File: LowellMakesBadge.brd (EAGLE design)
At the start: 51.9 x 52 mm, 2 parts

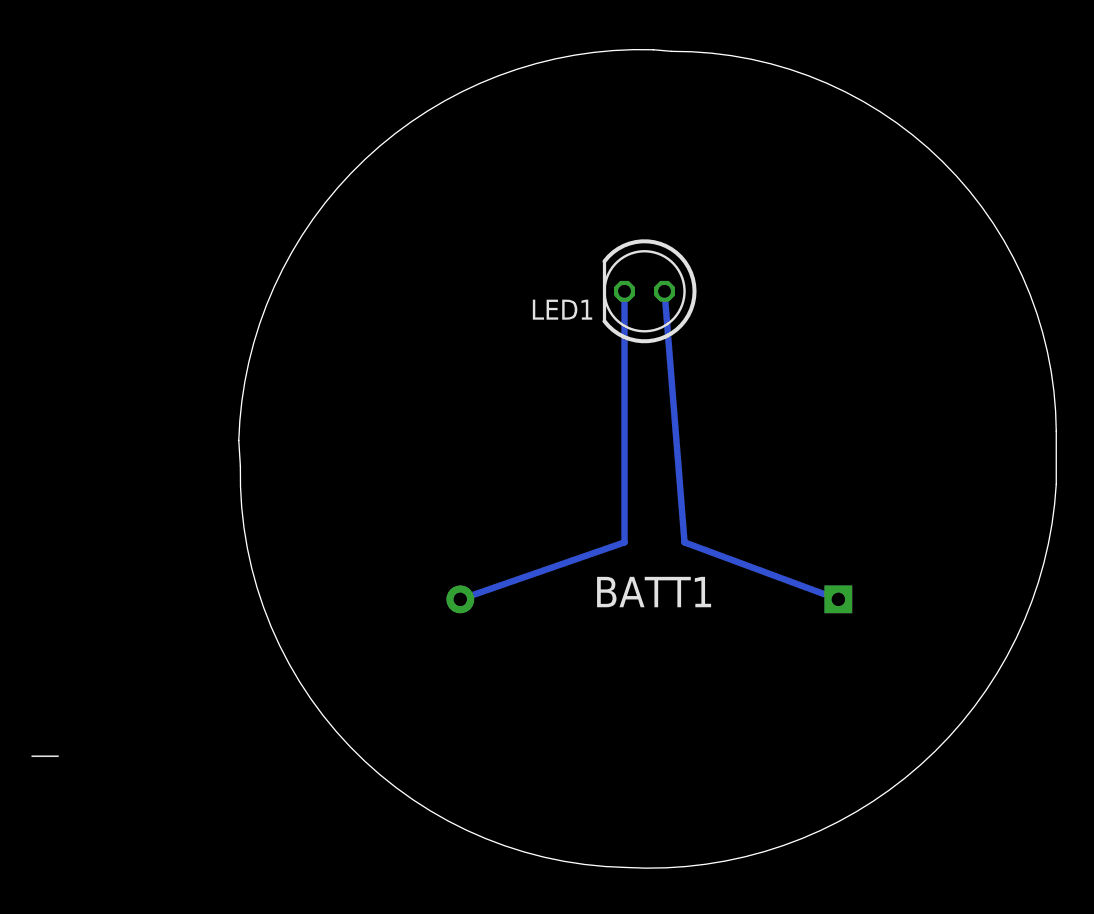
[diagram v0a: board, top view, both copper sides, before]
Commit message: Adding next version from @sajingeo including a 3d model
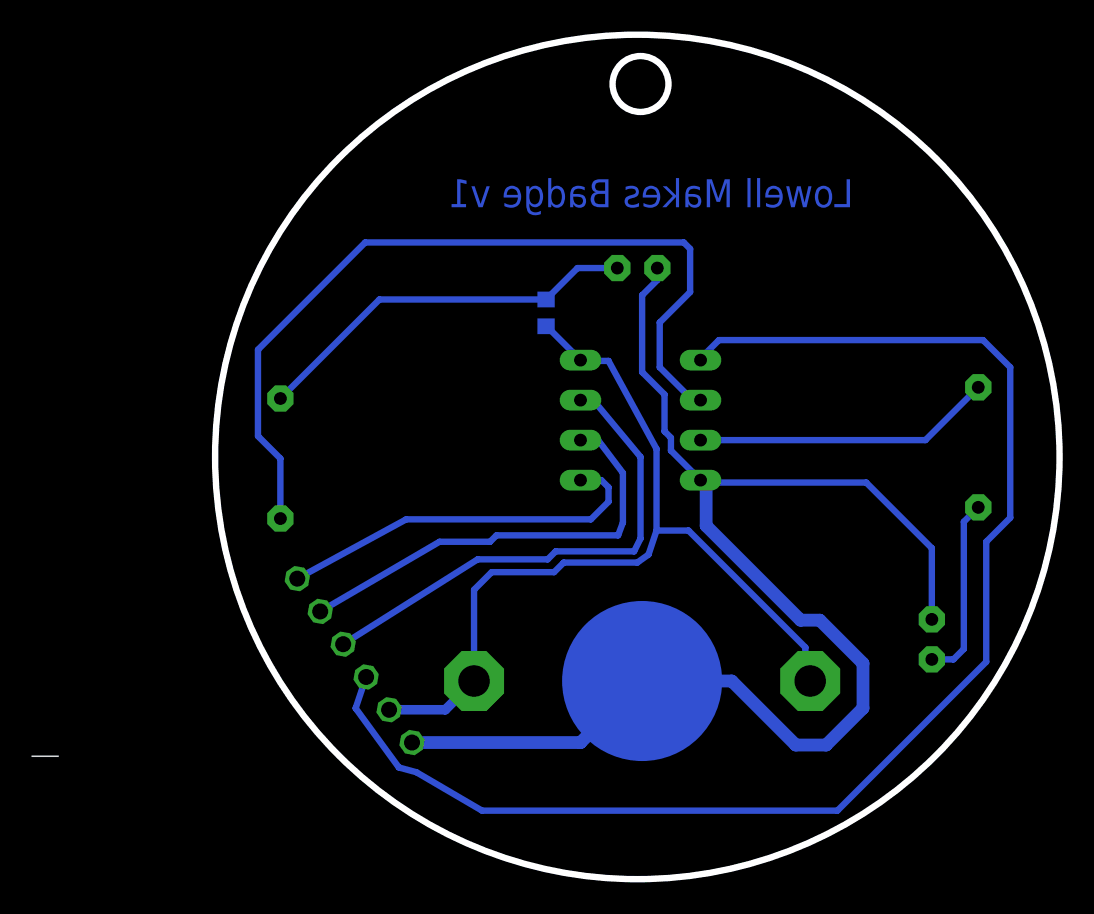
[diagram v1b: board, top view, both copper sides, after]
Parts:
- removed BATT1: FKIT-COIN_CELLLIR2450-H, SparkFun-Electromechanical:FKIT-LIR2450-H
- added IC1: TINY10P, atmel:DIL08
- added JP1: (no value), adafruit:1X06
- added LED2: (no value), adafruit:LED5MM
- added R1, R3: (no value), adafruit:0204/7
- added R2: (no value), adafruit:R0603
- added U$1: (no value), adafruit:CR2032-THRU
- LED1: device led:LED5MM -> adafruit:LED5MM
- moved LED1 1.54 mm to (51.6, 48.5), flipped to the bottom
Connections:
- removed net N$1: BATT1.POS, LED1.A
- new net N$2: LED2.A, R1.1
- new net N$3: IC1.2, R3.2
- new net N$4: LED1.A, R2.1, R3.1
- new net N$5: IC1.3, R1.2
- new net N$6: IC1.5, JP1.1
- new net N$7: IC1.6, JP1.2
- new net N$8: IC1.7, JP1.3
- new net N$9: IC1.1, JP1.4
- new net VCC: IC1.8, JP1.5, R2.2, U$1.+1, U$1.+2
- net GND: now also IC1.4, JP1.6, LED2.K, U$1.-; no longer BATT1.NEG
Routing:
- net N$9: track 0.00 -> 88.9 mm
- net GND: track 27.0 -> 88.7 mm
- net VCC: track 0.00 -> 56.7 mm
- net N$3: track 0.00 -> 53.5 mm
- net N$8: track 0.00 -> 31.8 mm
- net N$7: track 0.00 -> 28.0 mm
- net N$1: track 26.4 -> 0.00 mm
- net N$4: track 0.00 -> 24.8 mm
- net N$6: track 0.00 -> 24.1 mm
- net N$5: track 0.00 -> 19.0 mm
- net N$2: track 0.00 -> 11.7 mm
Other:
- board size 51.9 x 52 mm -> 53.6 x 53.6 mm
- board text added: "Lowell Makes Badge v1"

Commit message: More updates from @sajingeo
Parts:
- IC1: value TINY10P -> TINY10S; device atmel:DIL08 -> atmel:SOIC8
- moved R3 6.95 mm to (34.7, 40.3), turned to 0 degrees
- moved R1 5.92 mm to (71.2, 42.6)
- moved LED2 4.25 mm to (69.2, 29.0)
- moved JP1 3.71 mm to (34.3, 27.2), turned to 245 degrees
- moved U$1 2.92 mm to (52.3, 25.1)
- moved R2 2.11 mm to (43.9, 44.7)
- moved IC1 1.75 mm to (52.5, 40.4)
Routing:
- net N$9: track 88.9 -> 52.1 mm
- net GND: track 88.7 -> 64.1 mm
- net VCC: track 56.7 -> 40.5 mm
- net N$4: track 24.8 -> 15.9 mm
- net N$3: track 53.5 -> 46.9 mm
- net N$6: track 24.1 -> 20.1 mm
- net N$8: track 31.8 -> 27.9 mm
- net N$7: track 28.0 -> 24.9 mm
- net N$5: track 19.0 -> 18.3 mm
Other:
- board size 53.6 x 53.6 mm -> 48.8 x 48.8 mm

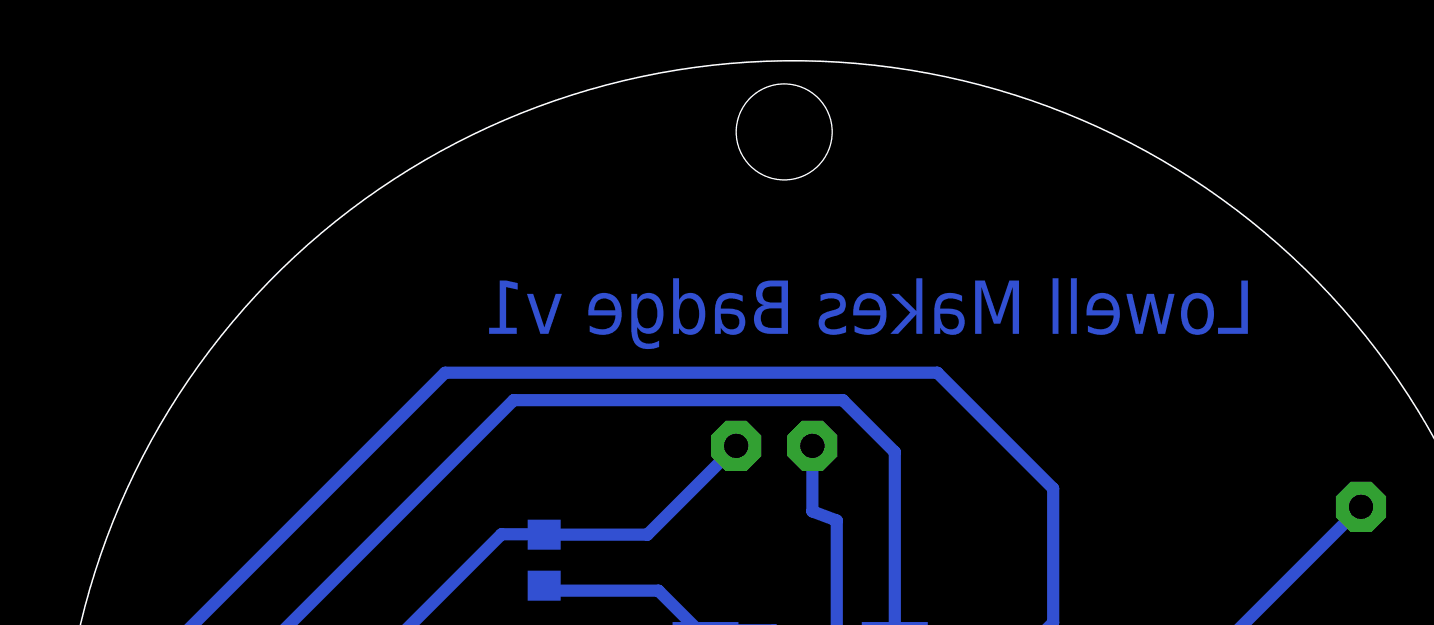
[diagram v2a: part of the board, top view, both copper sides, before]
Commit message: Updated board to change version from 1 to 2.0
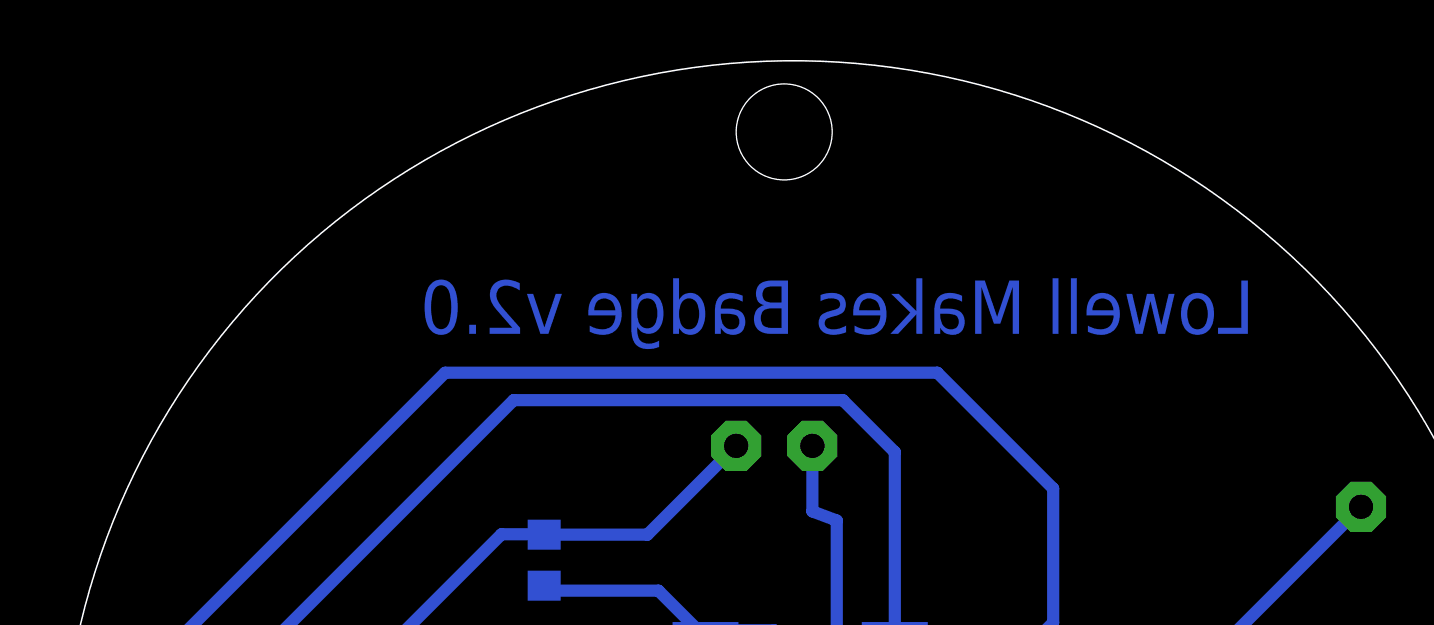
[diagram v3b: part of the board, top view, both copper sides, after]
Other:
- board text added: "Lowell Makes Badge v2.0"
- board text removed: "Lowell Makes Badge v1"
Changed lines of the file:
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@@
 <board>
 <plain>
-<text x="67.6148" y="52.197" size="1.778" layer="16" rot="MR0">Lowell Makes Badge v1</text>
+<text x="67.6148" y="52.197" size="1.778" layer="16" rot="MR0">Lowell Makes Badge v2.0</text>
 <circle x="52.2478" y="36.8808" radius="24.4191625" width="0.0508" layer="20"/>
 <rectangle x1="49.7205" y1="23.4315" x2="49.8475" y2="23.5585" layer="48"/>
